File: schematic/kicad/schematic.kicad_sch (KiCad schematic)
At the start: 14 parts, among them Q1 AO3401, SW1 SW_Nidec_CAS-120A1, U1 ESP32-C3, U2 MAX4466, U3 HW-373, U4 MT3608, U5 WS2812B

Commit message: Add gerbers
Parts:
- added J1, J2: Conn_01x02_Pin, Connector_JST:JST_XA_B02B-XASK-1_1x02_P2.50mm_Vertical, symbol Connector:Conn_01x02_Pin
- C1: footprint (none) -> Capacitor_THT:CP_Radial_D5.0mm_P2.50mm
- C2, C3, C6: footprint (none) -> Capacitor_THT:C_Disc_D5.0mm_W2.5mm_P5.00mm
- C4: footprint (none) -> Capacitor_THT:CP_Radial_D6.3mm_P2.50mm
- IN5822: footprint (none) -> Diode_THT:D_DO-27_P12.70mm_Horizontal
- R1: footprint (none) -> Resistor_THT:R_Axial_DIN0207_L6.3mm_D2.5mm_P7.62mm_Horizontal
- SW1: footprint Button_Switch_SMD:Nidec_Copal_CAS-120A -> Connector_JST:JST_XH_B2B-XH-A_1x02_P2.50mm_Vertical
- U1: footprint (none) -> components:ESP32-C3 Super Mini
- U2: footprint (none) -> Connector_JST:JST_XA_B03B-XASK-1-A_1x03_P2.50mm_Vertical
- U3: footprint (none) -> components:HW-373 Charge Controller
- U4: footprint (none) -> components:MT3608_Voltage_Booster
- U5: footprint (none) -> Connector_PinHeader_2.54mm:PinHeader_1x03_P2.54mm_Vertical; symbol components:WS2812B -> components:WS2812B_LED_Strip
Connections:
- net +5V: now also U3.1 (IN+); no longer U3. (OUT-)
- net +BATT: now also U3.5 (B+), J2.1 (Pin_1); no longer U3. (OUT-)
- net -BATT: now also U3.6 (B-), J2.2 (Pin_2); no longer U3. (OUT-)
- net GND: now also C3.2, C4.2, U1.2 (GND), U2.2 (GND), U3.2 (IN-), U3.4 (OUT-), U4.2 (IN-), U4.4 (OUT-), U5.1 (GND); no longer U1. (D0), U2. (VCC), U3. (OUT-), U4. (OUT-), U5. (GND)
- net at C1.1, C2.1, SW1.1 (C): now also U4.1 (IN+), J1.1 (Pin_1); no longer U4. (OUT-)
- net at IN5822.1 (K), Q1.2 (S), SW1.2 (B): now also J1.2 (Pin_2)
- net at Q1.3 (D): now also U3.3 (OUT+); no longer U3. (OUT-)
- new net: C3.1, C4.1, C6.1, U1.1 (5V), U2.1 (VCC), U4.3 (OUT+), U5.3 (VCC)
- new net: U1.7 (D1), U5.2 (DIN)
- new net: U1.8 (D0), U2.3 (OUT)
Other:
- moved on the sheet: SW1

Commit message: Adjust pcb and schematic
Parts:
- added C5: 100nF, Capacitor_THT:C_Disc_D5.0mm_W2.5mm_P5.00mm, symbol Device:C
- added U6: AMS1117, Connector_PinHeader_2.54mm:PinHeader_1x03_P2.54mm_Vertical, symbol Regulator_Linear:AMS1117
- C1: value 100uF -> 470uF
- C4: value 470uF -> 100uF
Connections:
- net GND: now also C5.2, U6.1 (ADJ)
- net +5VA: now reaches C6.1, U1.1 (5V), U4.3 (OUT+), U5.3 (VCC)
- net +5VA: now also C1.1, C2.1, U6.3 (VI); no longer C3.1, C4.1, U2.1 (VCC)
- net at IN5822.1 (K), Q1.2 (S), SW1.2 (B): now also J1.1 (Pin_1); no longer J1.2 (Pin_2)
- new net: C5.1, U2.1 (VCC), U6.2 (VO)
- new net VD: C3.1, C4.1, J1.2 (Pin_2), SW1.1 (C), U4.1 (IN+)
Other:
- note added: "(5V in or battery)"
- note added: "Boost Circuit"
- note added: "ESP"
- note added: "Load Sharing Circuit"
- note added: "Load shared power"
- note added: "Stable 5V power"
- moved on the sheet: C1, C2, C3, C4, C6, IN5822, J1, J2, R1, SW1, U1, U2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

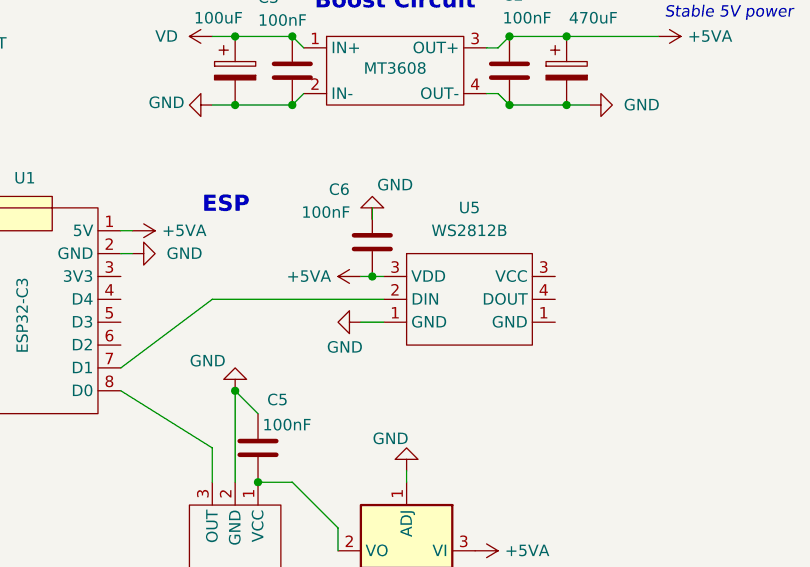
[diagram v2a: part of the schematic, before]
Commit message: Add extra signal resistor, update schematic and pcb
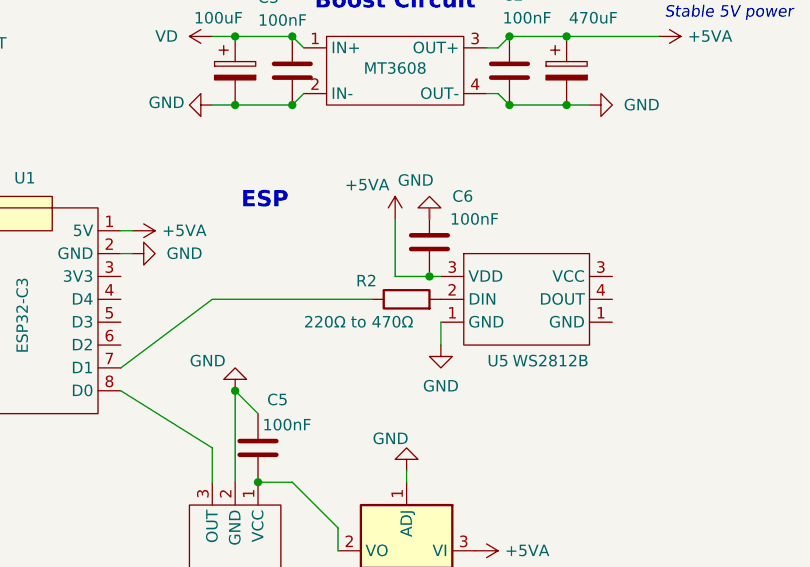
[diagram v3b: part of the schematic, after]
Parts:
- added R2: 220Ω to 470Ω, Resistor_THT:R_Axial_DIN0207_L6.3mm_D2.5mm_P7.62mm_Horizontal, symbol Device:R
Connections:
- net at U5.2 (DIN): now also R2.2; no longer U1.7 (D1)
- new net: R2.1, U1.7 (D1)
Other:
- moved on the sheet: C6, U5
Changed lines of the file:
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@@
 	(text "ESP"
 		(exclude_from_sim no)
-		(at 71.374 69.596 0)
+		(at 75.692 69.088 0)
 		(effects
 			(font
@@
 	)
 	(junction
-		(at 87.63 77.47)
+		(at 93.98 77.47)
 		(diameter 0)
 		(color 0 0 0 0)
@@
 	(wire
 		(pts
+			(xy 90.17 77.47) (xy 93.98 77.47)
+		)
+		(stroke
+			(width 0)
+			(type default)
+		)
+	)
+	(wire
+		(pts
 			(xy 72.39 58.42) (xy 78.74 58.42)
 		)
@@
 	(wire
 		(pts
-			(xy 87.63 71.12) (xy 87.63 69.85)
+			(xy 93.98 71.12) (xy 93.98 69.85)
 		)
 		(stroke
@@
 	(wire
 		(pts
-			(xy 86.36 82.55) (xy 88.9 82.55)
-		)
-		(stroke
-			(width 0)
-			(type default)
-		)
-	)
-	(wire
-		(pts
 			(xy 69.85 50.8) (xy 72.39 50.8)
 		)
@@
 	(wire
 		(pts
+			(xy 95.25 85.09) (xy 95.25 82.55)
+		)
+		(stroke
+			(width 0)
+			(type default)
+		)
+	)
+	(wire
+		(pts
 			(xy 83.82 107.95) (xy 83.82 105.41)
 		)
@@
 	(wire
 		(pts
+			(xy 90.17 71.12) (xy 90.17 77.47)
+		)
+		(stroke
+			(width 0)
+			(type default)
+		)
+	)
+	(wire
+		(pts
 			(xy 59.69 87.63) (xy 69.85 80.01)
 		)
@@
 	(wire
 		(pts
-			(xy 87.63 77.47) (xy 88.9 77.47)
-		)
-		(stroke
-			(width 0)
-			(type default)
-		)
-	)
-	(wire
-		(pts
-			(xy 87.63 77.47) (xy 86.36 77.47)
+			(xy 93.98 77.47) (xy 95.25 77.47)
+		)
+		(stroke
+			(width 0)
+			(type default)
+		)
+	)
+	(wire
+		(pts
+			(xy 69.85 80.01) (xy 87.63 80.01)
 		)
 		(stroke
@@
 		(pts
 			(xy 86.36 27.94) (xy 86.36 33.02)
-		)
-		(stroke
-			(width 0)
-			(type default)
-		)
-	)
-	(wire
-		(pts
-			(xy 88.9 80.01) (xy 69.85 80.01)
 		)
 		(stroke
@@
 	(symbol
 		(lib_id "components:WS2812B_LED_Strip")
-		(at 97.79 74.93 0)
+		(at 104.14 74.93 0)
 		(unit 1)
 		(exclude_from_sim no)
@@
 		(dnp no)
 		(property "Reference" "U5"
-			(at 98.425 69.85 0)
+			(at 101.6 86.868 0)
 			(effects
 				(font
@@
 		)
 		(property "Value" "WS2812B"
-			(at 98.425 72.39 0)
+			(at 107.442 86.868 0)
 			(effects
 				(font
@@
 		)
 		(property "Footprint" "Connector_PinHeader_2.54mm:PinHeader_1x03_P2.54mm_Vertical"
-			(at 97.79 74.93 0)
+			(at 104.14 74.93 0)
 			(effects
 				(font
@@
 		)
 		(property "Datasheet" ""
-			(at 97.79 74.93 0)
+			(at 104.14 74.93 0)
 			(effects
 				(font
@@
 		)
 		(property "Description" ""
-			(at 97.79 74.93 0)
+			(at 104.14 74.93 0)
 			(effects
 				(font
@@
 	(symbol
 		(lib_id "Device:C")
-		(at 87.63 73.66 180)
+		(at 93.98 73.66 180)
 		(unit 1)
 		(exclude_from_sim no)
@@
 		(dnp no)
 		(property "Reference" "C6"
-			(at 82.804 67.818 0)
+			(at 96.52 68.58 0)
 			(effects
 				(font
@@
 		)
 		(property "Value" "100nF"
-			(at 79.756 70.358 0)
+			(at 96.266 71.12 0)
 			(effects
 				(font
@@
 		)
 		(property "Footprint" "Capacitor_THT:C_Disc_D5.0mm_W2.5mm_P5.00mm"
-			(at 86.6648 69.85 0)
+			(at 93.0148 69.85 0)
 			(effects
 				(font
@@
 		)
 		(property "Datasheet" "~"
-			(at 87.63 73.66 0)
+			(at 93.98 73.66 0)
 			(effects
 				(font
@@
 		)
 		(property "Description" "Unpolarized capacitor"
-			(at 87.63 73.66 0)
+			(at 93.98 73.66 0)
 			(effects
 				(font
@@
 	(symbol
 		(lib_id "power:GND")
-		(at 87.63 71.12 180)
+		(at 93.98 71.12 180)
 		(unit 1)
 		(exclude_from_sim no)
@@
 		(dnp no)
 		(property "Reference" "#PWR017"
-			(at 87.63 64.77 0)
+			(at 93.98 64.77 0)
 			(effects
 				(font
@@
 		)
 		(property "Value" "GND"
-			(at 90.17 67.31 0)
+			(at 92.456 66.802 0)
 			(effects
 				(font
@@
 		)
 		(property "Footprint" ""
-			(at 87.63 71.12 0)
+			(at 93.98 71.12 0)
 			(effects
 				(font
@@
 		)
 		(property "Datasheet" ""
-			(at 87.63 71.12 0)
+			(at 93.98 71.12 0)
 			(effects
 				(font
@@
 		)
 		(property "Description" "Power symbol creates a global label with name \"GND\" , ground"
-			(at 87.63 71.12 0)
+			(at 93.98 71.12 0)
 			(effects
 				(font
@@
 	(symbol
 		(lib_id "power:GND")
-		(at 86.36 82.55 270)
+		(at 95.25 85.09 0)
 		(unit 1)
 		(exclude_from_sim no)
@@
 		(dnp no)
 		(property "Reference" "#PWR07"
-			(at 80.01 82.55 0)
+			(at 95.25 91.44 0)
 			(effects
 				(font
@@
 		)
 		(property "Value" "GND"
-			(at 84.582 85.344 90)
+			(at 95.25 89.662 0)
 			(effects
 				(font
@@
 		)
 		(property "Footprint" ""
-			(at 86.36 82.55 0)
+			(at 95.25 85.09 0)
 			(effects
 				(font
@@
 		)
 		(property "Datasheet" ""
-			(at 86.36 82.55 0)
+			(at 95.25 85.09 0)
 			(effects
 				(font
@@
 		)
 		(property "Description" "Power symbol creates a global label with name \"GND\" , ground"
-			(at 86.36 82.55 0)
+			(at 95.25 85.09 0)
 			(effects
 				(font
@@
 	(symbol
 		(lib_id "power:+5VA")
-		(at 86.36 77.47 90)
+		(at 90.17 71.12 0)
 		(unit 1)
 		(exclude_from_sim no)
@@
 		(dnp no)
 		(property "Reference" "#PWR016"
-			(at 90.17 77.47 0)
+			(at 90.17 74.93 0)
 			(effects
 				(font
@@
 		)
 		(property "Value" "+5VA"
-			(at 83.058 77.47 90)
+			(at 84.582 67.31 0)
 			(effects
 				(font
@@
 		)
 		(property "Footprint" ""
-			(at 86.36 77.47 0)
+			(at 90.17 71.12 0)
 			(effects
 				(font
@@
 		)
 		(property "Datasheet" ""
-			(at 86.36 77.47 0)
+			(at 90.17 71.12 0)
 			(effects
 				(font
@@
 		)
 		(property "Description" "Power symbol creates a global label with name \"+5VA\""
-			(at 86.36 77.47 0)
+			(at 90.17 71.12 0)
 			(effects
 				(font
@@
 					(unit 1)
 				)
+			)
+		)
+	)
+	(symbol
+		(lib_id "Device:R")
+		(at 91.44 80.01 90)
+		(unit 1)
+		(exclude_from_sim no)
+		(in_bom yes)
+		(on_board yes)
+		(dnp no)
+		(property "Reference" "R2"
+			(at 88.138 77.978 90)
+			(effects
+				(font
+					(size 1.27 1.27)
+				)
+				(justify left)
+			)
+		)
+		(property "Value" "220Ω to 470Ω"
+			(at 92.202 82.55 90)
+			(effects
+				(font
+					(size 1.27 1.27)
+				)
+				(justify left)
+			)
+		)
+		(property "Footprint" "Resistor_THT:R_Axial_DIN0207_L6.3mm_D2.5mm_P7.62mm_Horizontal"
+			(at 91.44 81.788 90)
+			(effects
+				(font
+					(size 1.27 1.27)
+				)
+				(hide yes)
+			)
+		)
+		(property "Datasheet" "~"
+			(at 91.44 80.01 0)
+			(effects
+				(font
+					(size 1.27 1.27)
+				)
+				(hide yes)
+			)
+		)
+		(property "Description" "Resistor"
+			(at 91.44 80.01 0)
+			(effects
+				(font
+					(size 1.27 1.27)
+				)
+				(hide yes)
+			)
+		)
+		(pin "2"
+		)
+		(pin "1"
+		)
+		(instances
+			(project "schematic"
+				(path "/1685a75f-db20-476f-a7be-a6eea2d7b7b5"
+					(reference "R2")
+					(unit 1)
+				)

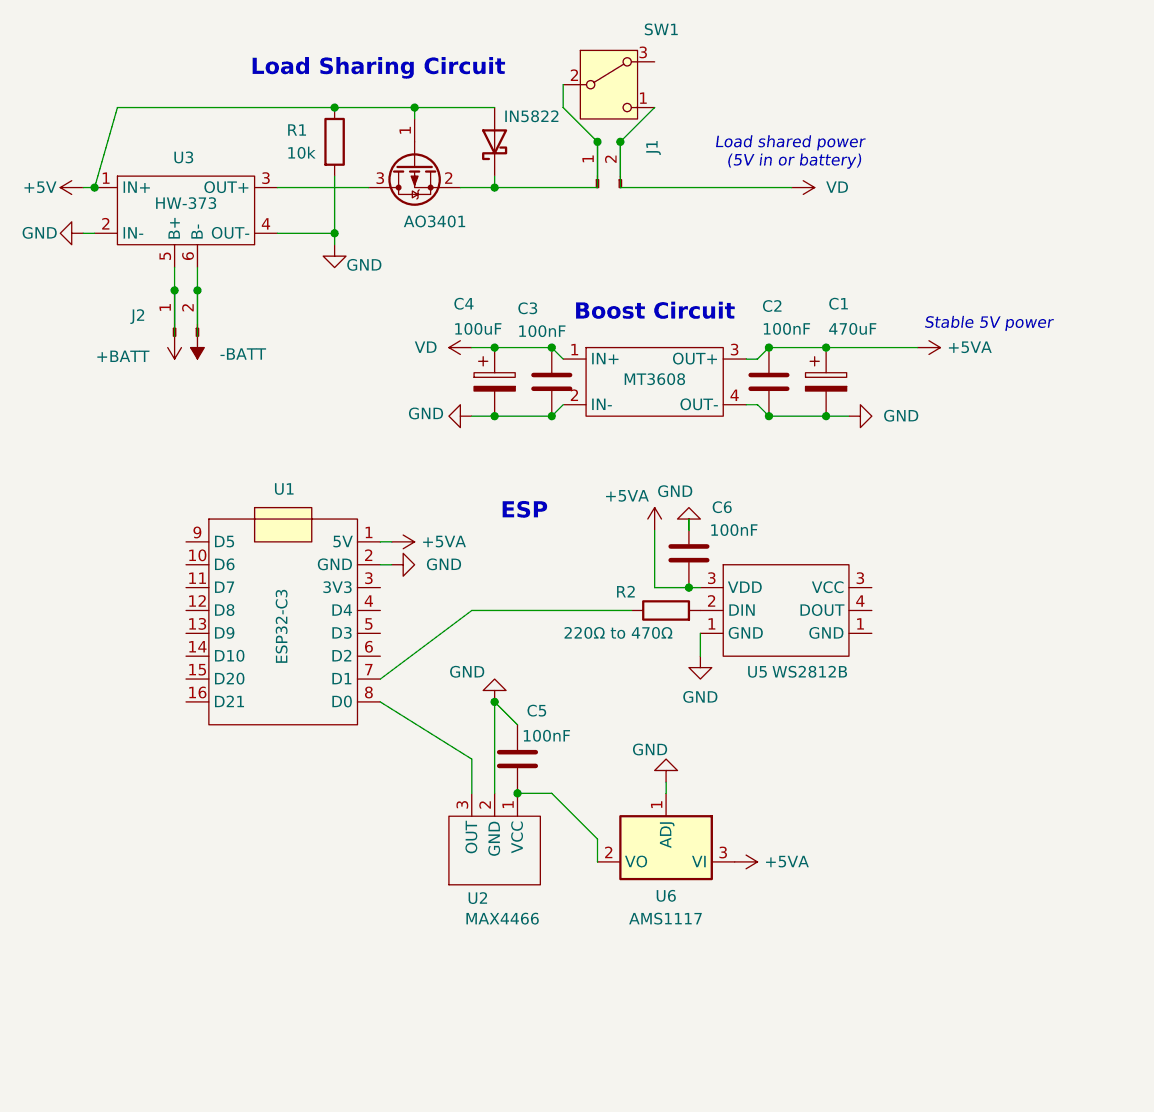
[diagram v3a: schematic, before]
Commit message: Add battery sense circuit
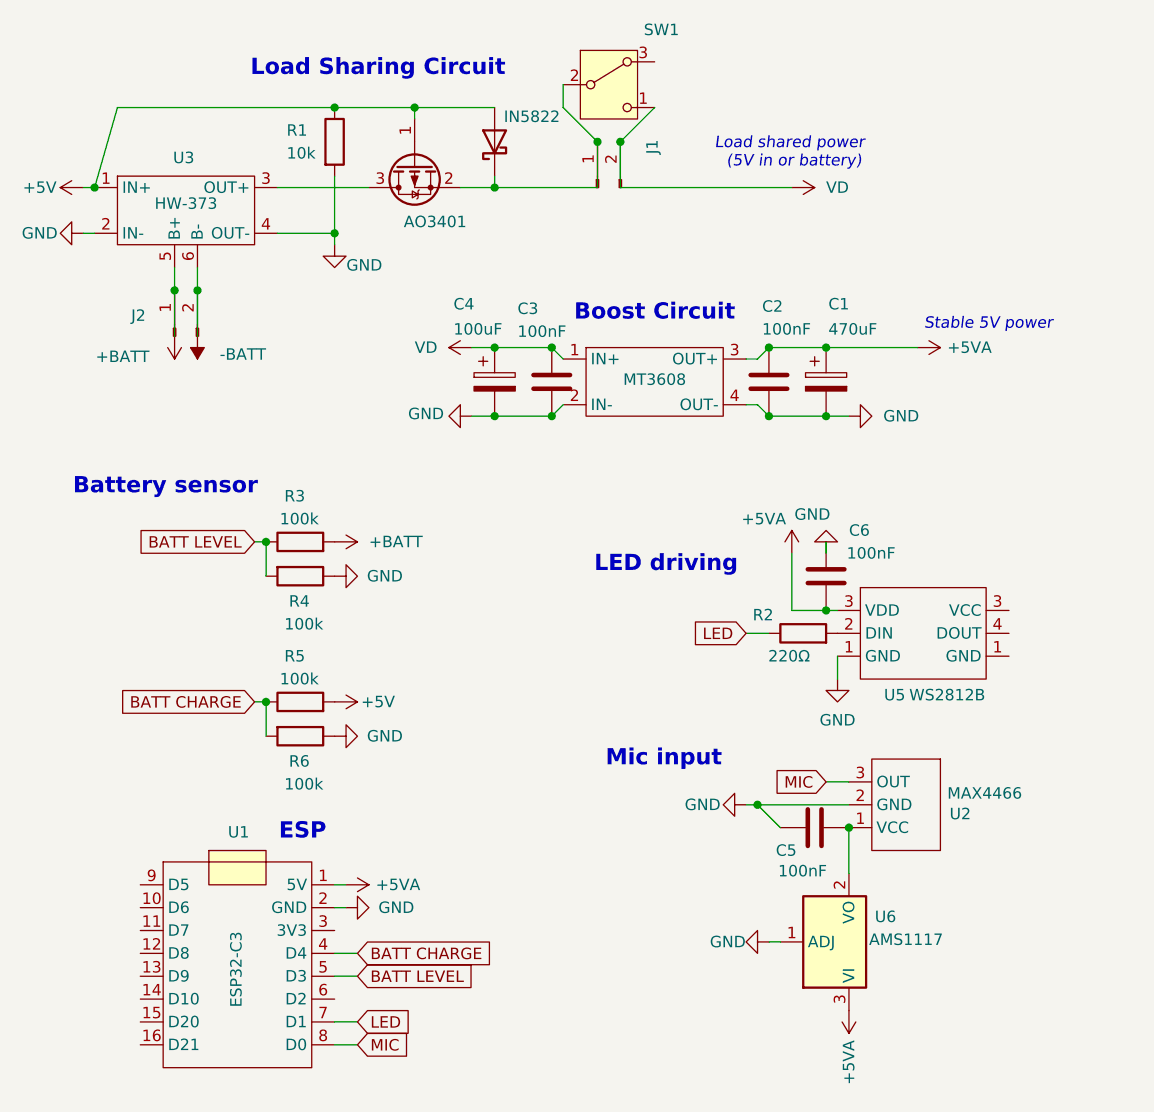
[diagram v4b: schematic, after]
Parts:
- added R3, R4, R5, R6: 100k, Resistor_THT:R_Axial_DIN0207_L6.3mm_D2.5mm_P7.62mm_Horizontal, symbol Device:R
- R2: value 220Ω to 470Ω -> 220Ω
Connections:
- net +5V: now also R5.2
- net +BATT: now also R3.2
- net GND: now also R4.1, R6.1
- net MIC: now reaches U1.8 (D0), U2.3 (OUT)
- net LED: now reaches R2.1, U1.7 (D1)
- net BATT CHARGE: now reaches U1.4 (D4)
- net BATT CHARGE: now also R5.1, R6.2
- net BATT LEVEL: now reaches U1.5 (D3)
- net BATT LEVEL: now also R3.1, R4.2
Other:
- note added: "Battery sensor"
- note added: "LED driving"
- note added: "Mic input"
- moved on the sheet: C5, C6, R2, U1, U2, U5, U6
